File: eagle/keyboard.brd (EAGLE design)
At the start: 100 x 100 mm, 72 parts, among them IC1 STC12C5616AD, Q1 12MHz

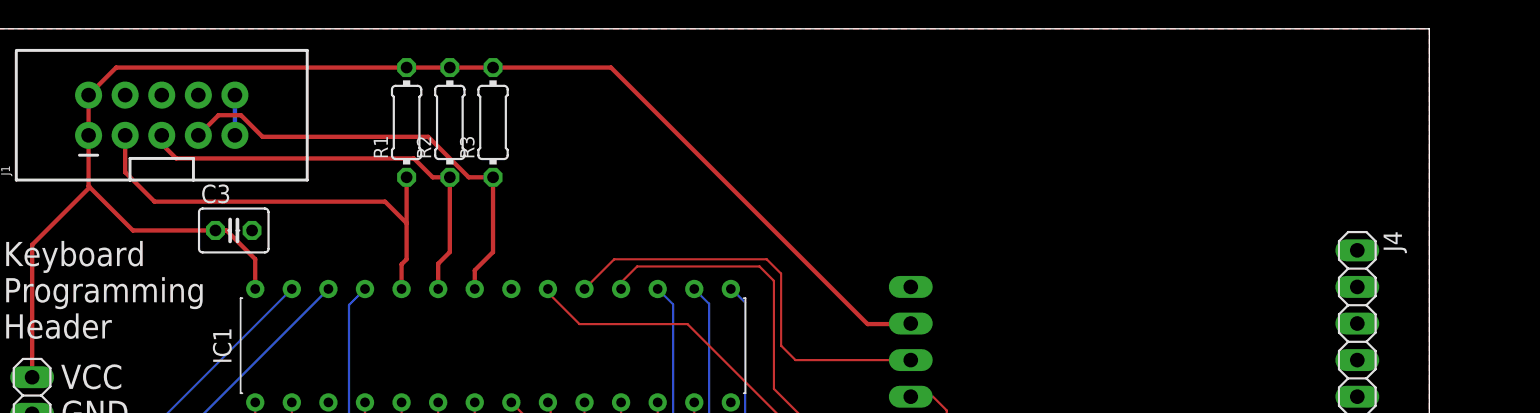
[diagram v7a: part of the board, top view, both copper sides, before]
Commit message: Add silkscreen
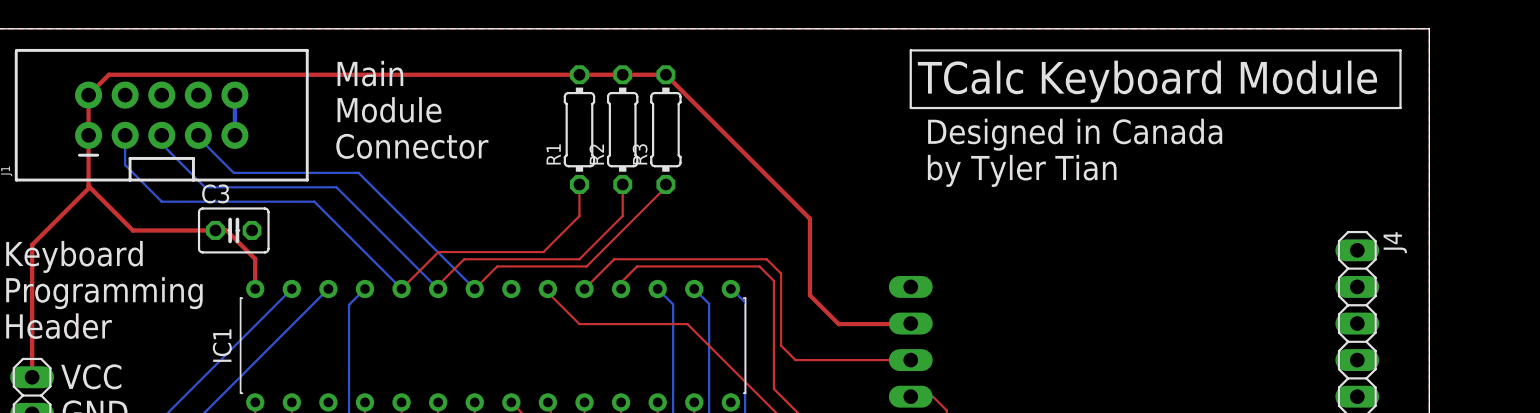
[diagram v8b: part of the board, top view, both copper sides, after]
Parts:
- moved R1 12.0 mm to (101.0, 93.0)
- moved R2 12.0 mm to (104.0, 93.0)
- moved R3 12.0 mm to (107.0, 93.0)
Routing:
- net SBDI_CLK: track 29.6 -> 41.2 mm
- net SBDI_EN: track 31.5 -> 41.5 mm
- net SBDI_DAT: track 31.1 -> 40.1 mm
- net VCC: track 102.3 -> 105.0 mm
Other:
- board text added: "Designed in Canada by Tyler Tian"
- board text added: "Main Module Connector"
- board text added: "TCalc Keyboard Module"
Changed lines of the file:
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@@
 Programming
 Header</text>
+<text x="84" y="91" size="1.6764" layer="21">Main
+Module
+Connector</text>
+<wire x1="124" y1="98.5" x2="158" y2="98.5" width="0.1524" layer="21"/>
+<wire x1="158" y1="98.5" x2="158" y2="94.5" width="0.1524" layer="21"/>
+<wire x1="158" y1="94.5" x2="124" y2="94.5" width="0.1524" layer="21"/>
+<wire x1="124" y1="94.5" x2="124" y2="98.5" width="0.1524" layer="21"/>
+<text x="125" y="89.5" size="1.6764" layer="21">Designed in Canada
+by Tyler Tian</text>
+<text x="124.5" y="95.5" size="2.2" layer="21">TCalc Keyboard Module</text>
 </plain>
 <attributes>
@@
 <attribute name="VALUE" x="93.987" y="72.71" size="1.27" layer="27" ratio="10" rot="R180"/>
 </element>
-<element name="R1" library="rcl" library_urn="urn:adsk.eagle:library:334" package="0204/7" package3d_urn="urn:adsk.eagle:package:23498/1" value="1K" x="89" y="93.5" smashed="yes" rot="R90">
-<attribute name="NAME" x="87.7046" y="90.96" size="0.9906" layer="25" ratio="10" rot="R90"/>
-<attribute name="SPICEPREFIX" value="R" x="194.41" y="153.19" size="1.778" layer="27" rot="R90" display="off"/>
-<attribute name="VALUE" x="89.4826" y="91.8744" size="0.9906" layer="27" ratio="10" rot="R90"/>
-</element>
-<element name="R2" library="rcl" library_urn="urn:adsk.eagle:library:334" package="0204/7" package3d_urn="urn:adsk.eagle:package:23498/1" value="1K" x="92" y="93.5" smashed="yes" rot="R90">
-<attribute name="NAME" x="90.7046" y="90.96" size="0.9906" layer="25" ratio="10" rot="R90"/>
-<attribute name="SPICEPREFIX" value="R" x="197.41" y="163.35" size="1.778" layer="27" rot="R90" display="off"/>
-<attribute name="VALUE" x="92.4826" y="91.8744" size="0.9906" layer="27" ratio="10" rot="R90"/>
-</element>
-<element name="R3" library="rcl" library_urn="urn:adsk.eagle:library:334" package="0204/7" package3d_urn="urn:adsk.eagle:package:23498/1" value="1K" x="95" y="93.5" smashed="yes" rot="R90">
-<attribute name="NAME" x="93.7046" y="90.96" size="0.9906" layer="25" ratio="10" rot="R90"/>
-<attribute name="SPICEPREFIX" value="R" x="200.41" y="173.51" size="1.778" layer="27" rot="R90" display="off"/>
-<attribute name="VALUE" x="95.4826" y="91.8744" size="0.9906" layer="27" ratio="10" rot="R90"/>
+<element name="R1" library="rcl" library_urn="urn:adsk.eagle:library:334" package="0204/7" package3d_urn="urn:adsk.eagle:package:23498/1" value="1K" x="101" y="93" smashed="yes" rot="R90">
+<attribute name="NAME" x="99.7046" y="90.46" size="0.9906" layer="25" ratio="10" rot="R90"/>
+<attribute name="SPICEPREFIX" value="R" x="206.41" y="152.69" size="1.778" layer="27" rot="R90" display="off"/>
+<attribute name="VALUE" x="101.4826" y="91.3744" size="0.9906" layer="27" ratio="10" rot="R90"/>
+</element>
+<element name="R2" library="rcl" library_urn="urn:adsk.eagle:library:334" package="0204/7" package3d_urn="urn:adsk.eagle:package:23498/1" value="1K" x="104" y="93" smashed="yes" rot="R90">
+<attribute name="NAME" x="102.7046" y="90.46" size="0.9906" layer="25" ratio="10" rot="R90"/>
+<attribute name="SPICEPREFIX" value="R" x="209.41" y="162.85" size="1.778" layer="27" rot="R90" display="off"/>
+<attribute name="VALUE" x="104.4826" y="91.3744" size="0.9906" layer="27" ratio="10" rot="R90"/>
+</element>
+<element name="R3" library="rcl" library_urn="urn:adsk.eagle:library:334" package="0204/7" package3d_urn="urn:adsk.eagle:package:23498/1" value="1K" x="107" y="93" smashed="yes" rot="R90">
+<attribute name="NAME" x="105.7046" y="90.46" size="0.9906" layer="25" ratio="10" rot="R90"/>
+<attribute name="SPICEPREFIX" value="R" x="212.41" y="173.01" size="1.778" layer="27" rot="R90" display="off"/>
+<attribute name="VALUE" x="107.4826" y="91.3744" size="0.9906" layer="27" ratio="10" rot="R90"/>
 </element>
 <element name="S1" library="switch-omron" library_urn="urn:adsk.eagle:library:377" package="B3F-10XX" package3d_urn="urn:adsk.eagle:package:27496/1" value="" x="65" y="56" smashed="yes" rot="R90">
@@
 <contactref element="R1" pad="1"/>
 <contactref element="J1" pad="3"/>
-<wire x1="88.65" y1="81.937" x2="88.65" y2="83.65" width="0.3" layer="1"/>
-<wire x1="88.65" y1="83.65" x2="89" y2="84" width="0.3" layer="1"/>
-<wire x1="89" y1="84" x2="89" y2="86.5" width="0.3" layer="1"/>
-<wire x1="89" y1="86.5" x2="89" y2="89.69" width="0.3" layer="1"/>
-<wire x1="69.46" y1="92.603" x2="69.46" y2="90.04" width="0.3" layer="1"/>
-<wire x1="69.46" y1="90.04" x2="71.5" y2="88" width="0.3" layer="1"/>
-<wire x1="87.5" y1="88" x2="89" y2="86.5" width="0.3" layer="1"/>
-<wire x1="71.5" y1="88" x2="87.5" y2="88" width="0.3" layer="1"/>
+<wire x1="88.65" y1="81.937" x2="91.213" y2="84.5" width="0.1524" layer="1"/>
+<wire x1="98.5" y1="84.5" x2="101" y2="87" width="0.1524" layer="1"/>
+<wire x1="101" y1="87" x2="101" y2="89.19" width="0.1524" layer="1"/>
+<wire x1="91.213" y1="84.5" x2="98.5" y2="84.5" width="0.1524" layer="1"/>
+<wire x1="88.65" y1="81.937" x2="82.587" y2="88" width="0.1524" layer="16"/>
+<wire x1="82.587" y1="88" x2="72" y2="88" width="0.1524" layer="16"/>
+<wire x1="72" y1="88" x2="69.46" y2="90.54" width="0.1524" layer="16"/>
+<wire x1="69.46" y1="90.54" x2="69.46" y2="92.603" width="0.1524" layer="16"/>
 </signal>
 <signal name="SBDI_CLK">
@@
 <contactref element="R2" pad="1"/>
 <contactref element="J1" pad="5"/>
-<wire x1="91.19" y1="81.937" x2="91.19" y2="83.69" width="0.3" layer="1"/>
-<wire x1="91.19" y1="83.69" x2="92" y2="84.5" width="0.3" layer="1"/>
-<wire x1="92" y1="84.5" x2="92" y2="89.69" width="0.3" layer="1"/>
-<wire x1="92" y1="89.69" x2="90.81" y2="89.69" width="0.3" layer="1"/>
-<wire x1="89.5" y1="91" x2="73" y2="91" width="0.3" layer="1"/>
-<wire x1="73" y1="91" x2="72" y2="92" width="0.3" layer="1"/>
-<wire x1="72" y1="92" x2="72" y2="92.603" width="0.3" layer="1"/>
-<wire x1="90.81" y1="89.69" x2="89.5" y2="91" width="0.3" layer="1"/>
+<wire x1="104" y1="89.19" x2="104" y2="87" width="0.1524" layer="1"/>
+<wire x1="104" y1="87" x2="101" y2="84" width="0.1524" layer="1"/>
+<wire x1="101" y1="84" x2="93" y2="84" width="0.1524" layer="1"/>
+<wire x1="93" y1="84" x2="91.19" y2="82.19" width="0.1524" layer="1"/>
+<wire x1="91.19" y1="82.19" x2="91.19" y2="81.937" width="0.1524" layer="1"/>
+<wire x1="91.19" y1="81.937" x2="84.127" y2="89" width="0.1524" layer="16"/>
+<wire x1="84.127" y1="89" x2="75" y2="89" width="0.1524" layer="16"/>
+<wire x1="75" y1="89" x2="72" y2="92" width="0.1524" layer="16"/>
+<wire x1="72" y1="92" x2="72" y2="92.603" width="0.1524" layer="16"/>
 </signal>
 <signal name="SBDI_DAT">
@@
 <contactref element="R3" pad="1"/>
 <contactref element="J1" pad="7"/>
-<wire x1="93.73" y1="81.937" x2="93.73" y2="83.23" width="0.3" layer="1"/>
-<wire x1="93.73" y1="83.23" x2="95" y2="84.5" width="0.3" layer="1"/>
-<wire x1="95" y1="84.5" x2="95" y2="89.69" width="0.3" layer="1"/>
-<wire x1="95" y1="89.69" x2="93.31" y2="89.69" width="0.3" layer="1"/>
-<wire x1="79" y1="92.5" x2="77.5" y2="94" width="0.3" layer="1"/>
-<wire x1="77.5" y1="94" x2="75.937" y2="94" width="0.3" layer="1"/>
-<wire x1="75.937" y1="94" x2="74.54" y2="92.603" width="0.3" layer="1"/>
-<wire x1="93.31" y1="89.69" x2="90.5" y2="92.5" width="0.3" layer="1"/>
-<wire x1="90.5" y1="92.5" x2="79" y2="92.5" width="0.3" layer="1"/>
+<wire x1="93.73" y1="81.937" x2="95.293" y2="83.5" width="0.1524" layer="1"/>
+<wire x1="107" y1="89" x2="107" y2="89.19" width="0.1524" layer="1"/>
+<wire x1="95.293" y1="83.5" x2="101.5" y2="83.5" width="0.1524" layer="1"/>
+<wire x1="101.5" y1="83.5" x2="107" y2="89" width="0.1524" layer="1"/>
+<wire x1="93.73" y1="81.937" x2="85.667" y2="90" width="0.1524" layer="16"/>
+<wire x1="85.667" y1="90" x2="77" y2="90" width="0.1524" layer="16"/>
+<wire x1="77" y1="90" x2="74.54" y2="92.46" width="0.1524" layer="16"/>
+<wire x1="74.54" y1="92.46" x2="74.54" y2="92.603" width="0.1524" layer="16"/>
 </signal>
 <signal name="XTAL2">
@@
 <wire x1="66.92" y1="95.397" x2="67" y2="95.317" width="0.1524" layer="1"/>
 <wire x1="63" y1="75.81" x2="63" y2="85" width="0.3" layer="1"/>
-<wire x1="89" y1="97.31" x2="92" y2="97.31" width="0.3" layer="1"/>
-<wire x1="92" y1="97.31" x2="95" y2="97.31" width="0.3" layer="1"/>
-<wire x1="66.92" y1="95.397" x2="68.833" y2="97.31" width="0.3" layer="1"/>
-<wire x1="68.833" y1="97.31" x2="89" y2="97.31" width="0.3" layer="1"/>
-<wire x1="95" y1="97.31" x2="103.19" y2="97.31" width="0.3" layer="1"/>
-<wire x1="103.19" y1="97.31" x2="121" y2="79.5" width="0.3" layer="1"/>
-<wire x1="121" y1="79.5" x2="123.96" y2="79.5" width="0.3" layer="1"/>
+<wire x1="101" y1="96.81" x2="104" y2="96.81" width="0.3" layer="1"/>
+<wire x1="104" y1="96.81" x2="107" y2="96.81" width="0.3" layer="1"/>
+<wire x1="66.92" y1="95.397" x2="68.333" y2="96.81" width="0.3" layer="1"/>
+<wire x1="68.333" y1="96.81" x2="101" y2="96.81" width="0.3" layer="1"/>
 <wire x1="123.96" y1="79.5" x2="124" y2="79.54" width="0.6" layer="1"/>
 <wire x1="67" y1="89" x2="66.92" y2="89.08" width="0.3" layer="1"/>
@@
 <wire x1="76.5" y1="86" x2="78.49" y2="84.01" width="0.3" layer="1"/>
 <wire x1="78.49" y1="84.01" x2="78.49" y2="81.937" width="0.3" layer="1"/>
+<wire x1="107" y1="96.81" x2="117" y2="86.81" width="0.3" layer="1"/>
+<wire x1="117" y1="86.81" x2="117" y2="81.5" width="0.3" layer="1"/>
+<wire x1="117" y1="81.5" x2="119" y2="79.5" width="0.3" layer="1"/>
+<wire x1="119" y1="79.5" x2="123.96" y2="79.5" width="0.3" layer="1"/>
 </signal>
 <signal name="RXD/COL3">
